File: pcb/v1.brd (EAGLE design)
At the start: 92 x 80 mm, 61 parts, among them T1 MMBT3904, T2 MMBT3904, T3 MMBT3904, T4 MMBT3904

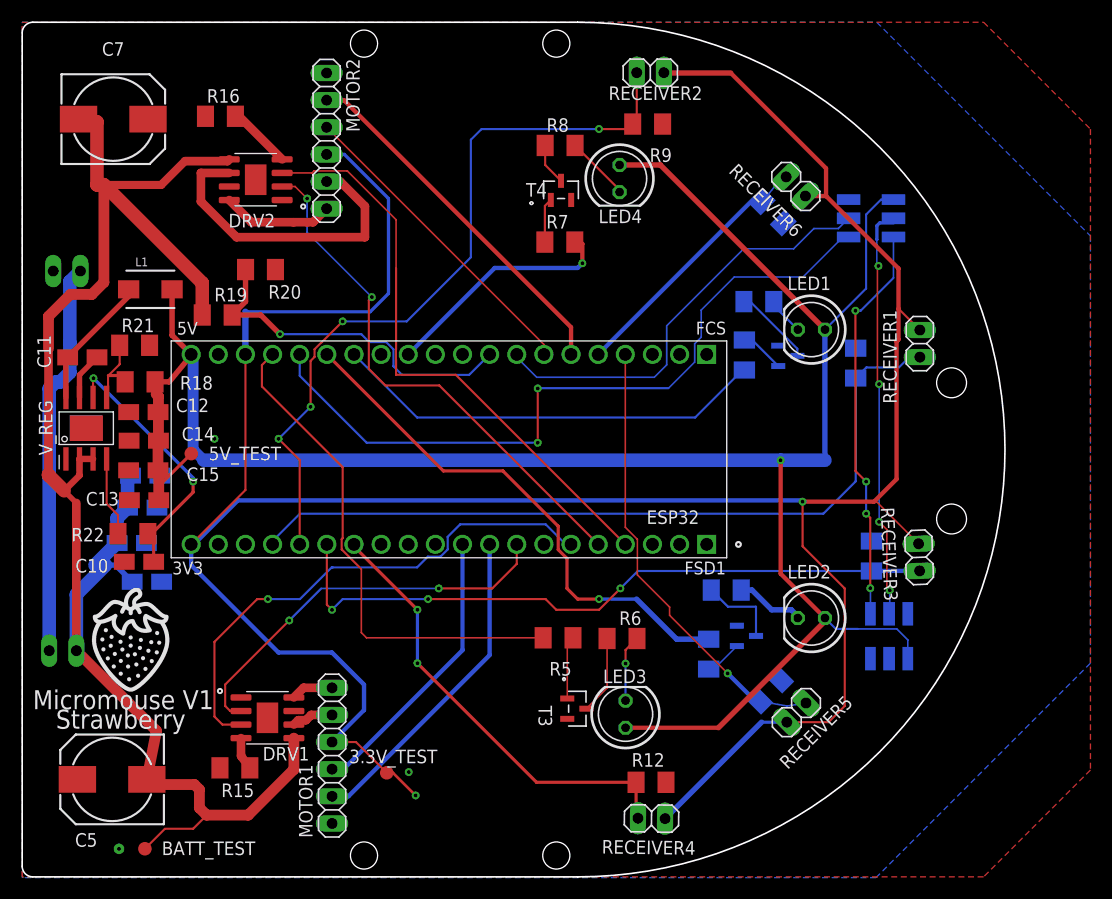
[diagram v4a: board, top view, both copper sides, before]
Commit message: Last minute touches to PCB Moved headers for motor and led to not interfere with nuts. Made ground plane solid instead of hatched. Fixed silkscreen overlap. Connected ground planes for top and bottom. Added dru for jlbpcb.
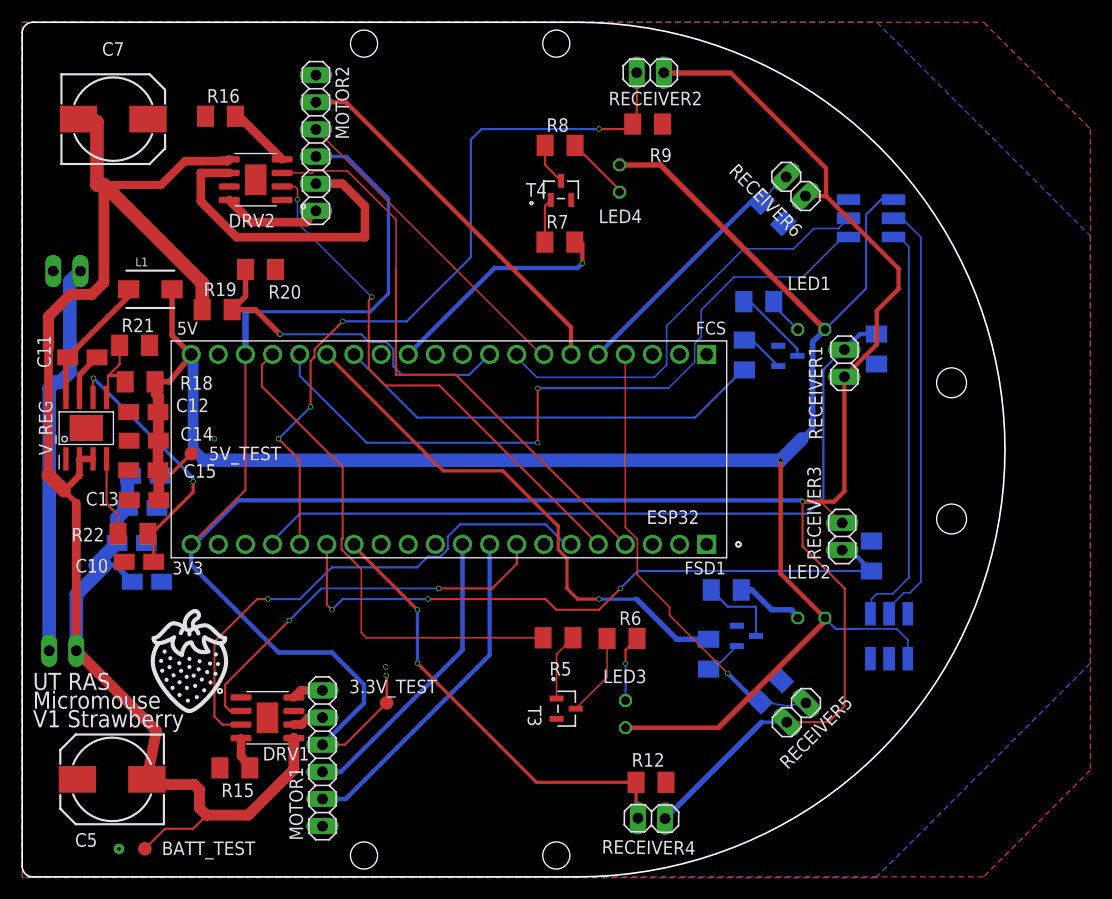
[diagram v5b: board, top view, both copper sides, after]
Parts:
- moved RECEIVER3 7.46 mm to (76.8, 31.9), turned to 270 degrees
- moved RECEIVER1 7.30 mm to (77.0, 48.1), turned to 90 degrees
- moved 3.3V_TEST 6.55 mm to (34.1, 16.3)
- moved R13 2.36 mm to (80.0, 49.4), turned to 90 degrees
- moved MOTOR2 1.02 mm to (27.5, 68.7)
- moved T3 1.00 mm to (51.0, 15.7)
- moved MOTOR1 0.93 mm to (28.1, 11.1)
- moved R19 0.50 mm to (18.3, 53.1)
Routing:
- net 3.3V: track 272.4 -> 261.3 mm
- net 5V: track 202.0 -> 199.6 mm
- net REC1: track 73.7 -> 71.9 mm
- net N$34: track 39.0 -> 40.1 mm, vias 4 -> 0
- net N$17: track 3.95 -> 2.95 mm
- net N$16: track 3.95 -> 2.95 mm
- net EN0B: track 26.7 -> 27.7 mm
- net EN0A: track 30.6 -> 31.6 mm
- net REC3: track 63.7 -> 62.7 mm
- net N$18: track 10.5 -> 9.56 mm
- net N$35: track 37.6 -> 38.6 mm, vias 4 -> 0
- net EN1A: track 34.2 -> 35.1 mm
- net N$19: track 29.5 -> 30.4 mm
- net BATT_POWER: track 156.7 -> 156.2 mm
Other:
- board text added: "Micromouse"
- board text added: "UT RAS"
- board text added: "V1 Strawberry"
- board text removed: "Micromouse V1"
- board text removed: "Strawberry"

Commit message: Changed PCB
Fixes #11
Fixes #10
Fixes #9
Fixes #8
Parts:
- removed 5V_TEST: PTR1B1,27, testpad:B1,27
- added C1, C2: 10uF, rcl:A/3216-18R
- added R17, R23: 10k, rcl:M1206
- added S1, S2: DTSM-6, switch-tact:DTSM-6
- added SW1: (no value), pinhead:1X02
- added V_REG2: (no value), pinhead:1X05
- C12, C13, C14, C15: value 10uF -> 22uF
- LED1, LED2, LED3, LED4: device led:LED5MM -> pinhead:1X02
- moved C6 36.1 mm to (22.8, 62.0), flipped to the top
- moved LED2 29.1 mm to (72.4, 53.3), turned to 0 degrees
- moved LED1 24.6 mm to (72.4, 26.7), turned to 0 degrees
- moved C3 23.5 mm to (22.9, 58.2), flipped to the top
- moved C4 18.9 mm to (21.5, 16.1), flipped to the top
- moved R15 10.3 mm to (14.4, 18.9)
- moved RECEIVER3 7.46 mm to (84.0, 29.9), turned to 272.2 degrees
- moved RECEIVER1 7.30 mm to (84.0, 49.9), turned to 270 degrees
- moved 3.3V_TEST 6.55 mm to (34.1, 9.74)
- moved MOTOR2 5.62 mm to (30.3, 63.8)
- moved DRV1 4.93 mm to (21.8, 19.7)
- moved T2 4.02 mm to (73.0, 45.0), flipped to the top, turned to 0 degrees
- moved LED4 4.01 mm to (58.4, 62.2), turned to 0 degrees
- moved MOTOR1 3.96 mm to (30.7, 14.1)
- moved R20 2.90 mm to (23.1, 54.1)
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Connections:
- removed net N$11: LED3.K, R6.2
- new net LED3: LED3.2, R6.2
- new net N$22: C2.+, S2.4
- new net N$3: BATT1.1, SW1.1
- new net N$4: C1.+, S1.4
- new net SW1: C1.-, ESP32.J2_7, R17.2, S1.1, S1.2
- new net SW2: C2.-, ESP32.J3_10, R23.2, S2.1, S2.2
- net 3.3V: now also ESP32.J3_17, S1.3, S2.3
- net 5V: now also LED1.1, LED2.1, LED3.1, LED4.1, V_REG2.5; no longer 5V_TEST.TP, LED1.A, LED2.A, LED3.A, LED4.A
- net BATT_POWER: now also SW1.2, V_REG2.1, V_REG2.2; no longer BATT1.1
- net EM1: now also ESP32.J2_11; no longer ESP32.J3_14
- net EM3: now also ESP32.J3_11; no longer ESP32.J3_17
- net EM4: now also ESP32.J3_13; no longer ESP32.J3_12
- net GND: now also DRV1.P$1, DRV2.P$1, R17.1, R23.1, V_REG.P$1, V_REG.P$2, V_REG2.3, V_REG2.4
- net N$14: now also LED4.2; no longer LED4.K
- net N$6: now also LED2.2; no longer LED1.K
- net N$8: now also LED1.2; no longer LED2.K
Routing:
- net SW1: track 0.00 -> 65.7 mm
- net SW2: track 0.00 -> 47.0 mm, vias 0 -> 1
- net 3.3V: track 261.3 -> 238.2 mm
- net V_SENSE: track 32.6 -> 54.0 mm
- net EM3: track 47.6 -> 30.7 mm, vias 0 -> 3
- net BATT_POWER: track 156.2 -> 143.2 mm, vias 0 -> 8
- net PG: track 7.44 -> 18.7 mm, vias 0 -> 1
- net N$19: track 30.4 -> 19.7 mm, vias 0 -> 1
- net LED_SIG: track 69.4 -> 59.1 mm, vias 2 -> 7
- net 5V: track 199.6 -> 190.9 mm, vias 1 -> 5
- net N$18: track 9.56 -> 17.4 mm, vias 0 -> 1
- net REC2: track 70.4 -> 63.1 mm, vias 4 -> 0
- net N$11: track 6.26 -> 0.00 mm
- net N$34: track 40.1 -> 46.4 mm
- net LED3: track 0.00 -> 6.18 mm
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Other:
- board text removed: "Micromouse"
- board text removed: "UT RAS"
- board text removed: "V1 Strawberry"

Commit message: Cosmetic Changes
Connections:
- net BATT_POWER: now also C5.+, C7.+; no longer C5.-, C7.-
- net GND: now also C5.-, C7.-; no longer C5.+, C7.+
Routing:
- net BATT_POWER: track 143.2 -> 146.0 mm
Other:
- board text added: "Micromouse 2019"
- board text added: "V1.1 Blueberry"
- board text removed: "/Users/vamsighorakavi/Downloads/strawberry(2).bmp"
